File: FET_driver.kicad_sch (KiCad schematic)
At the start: 48 parts, among them Q1 TPH3R704PL,L1Q, Q10 TPH3R704PL,L1Q, Q11 TPH3R704PL,L1Q, Q12 TPH3R704PL,L1Q, Q2 TPH3R704PL,L1Q, Q3 TPH3R704PL,L1Q, Q4 TPH3R704PL,L1Q, Q5 TPH3R704PL,L1Q, Q6 TPH3R704PL,L1Q, Q7 TPH3R704PL,L1Q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

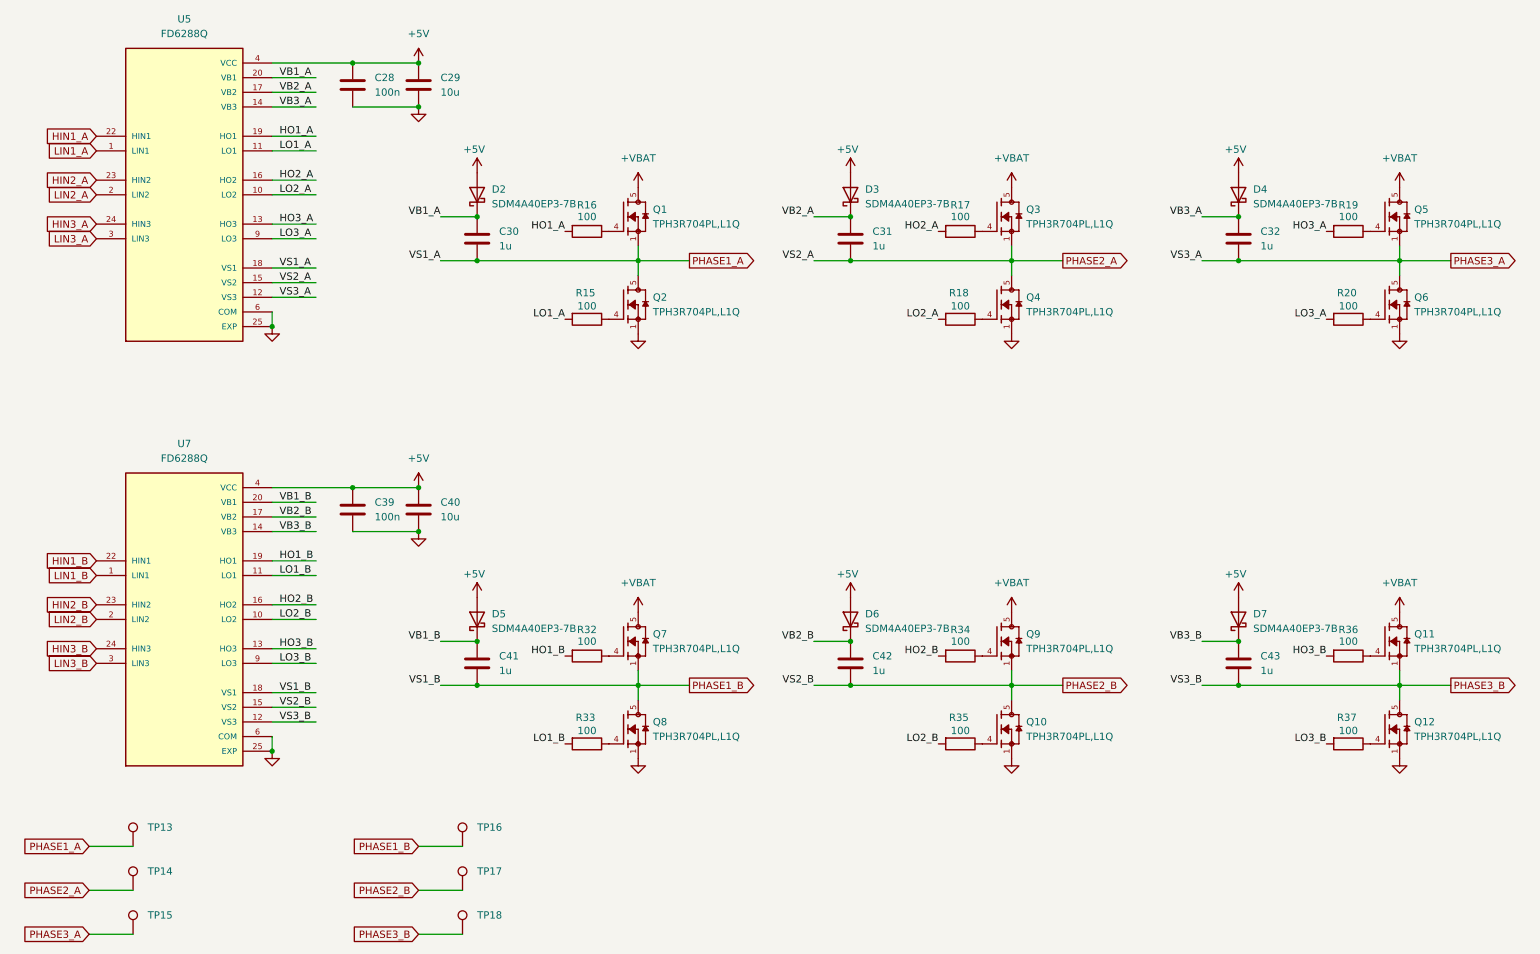
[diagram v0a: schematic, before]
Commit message: remove blind vias
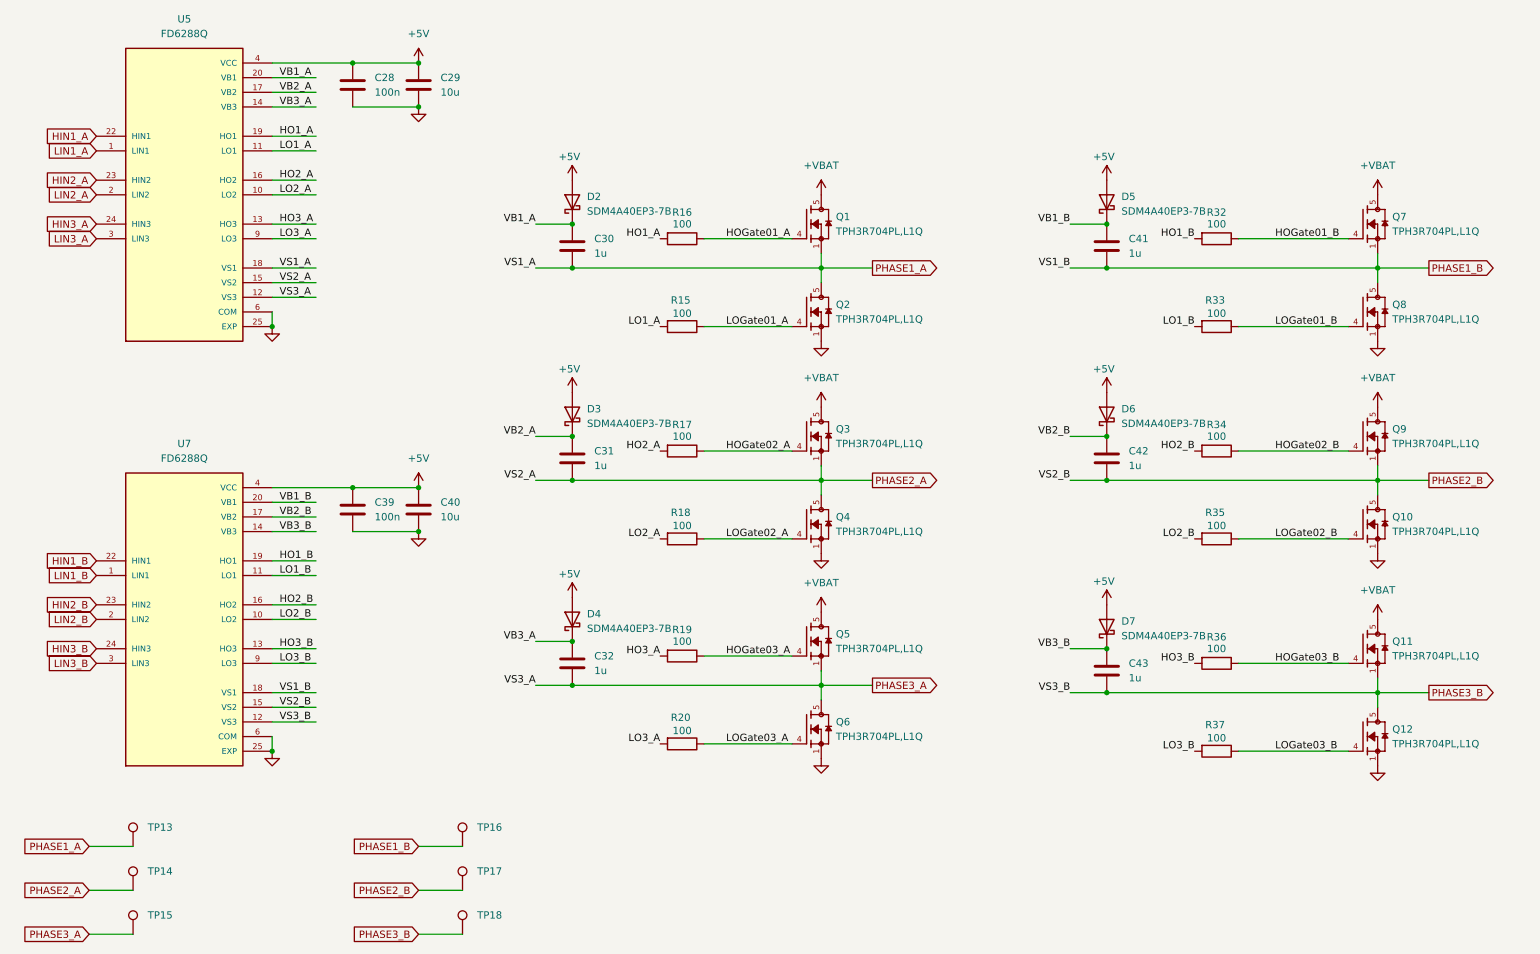
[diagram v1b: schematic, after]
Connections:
- net HOGate02_B: now reaches Q9.4, R34.1
- net LOGate02_B: now reaches Q10.4, R35.1
- net HOGate03_B: now reaches Q11.4, R36.1
- net HOGate02_A: now reaches Q3.4, R17.1
- net HOGate03_A: now reaches Q5.4, R19.1
- net LOGate03_A: now reaches Q6.4, R20.1
- net LOGate02_A: now reaches Q4.4, R18.1
- net LOGate01_A: now reaches Q2.4, R15.1
- net HOGate01_B: now reaches Q7.4, R32.1
- net LOGate01_B: now reaches Q8.4, R33.1
- net HOGate01_A: now reaches Q1.4, R16.1
- net LOGate03_B: now reaches Q12.4, R37.1
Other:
- moved on the sheet: C30, C31, C32, C41, C42, C43, D2, D3, D4, D5, D6, D7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
